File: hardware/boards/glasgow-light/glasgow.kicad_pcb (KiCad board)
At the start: 2 copper layers, 191 parts, among them J1 USB_C_USB2.0, J10 AUX, J2 IDC-Header_2x5_P2.54mm, J3 IDC-Header_2x5_P2.54mm, J4 Conn_01x02, U1 LM358_DFN, U10 SN74LVC1T45DCKR, U11 SN74LVC1T45DCKR, U12 INA180A2, U15 TPD3S014, U16 SN74LVC1T45DCKR, U17 SN74LVC1T45DCKR, U18 SN74LVC1T45DCKR, U19 PCA6408APW, U31 TPS73101DBV, U36 TLV73312PQDRVR, U4 SN74LVC1T45DCKR, U5 ICE40UP5K-SG48ITR, U6 SN74LVC1T45DCKR, U7 GD32VF103, U8 TLV75533PDRVR, U9 SN74LVC1T45DCKR, Y1 8M

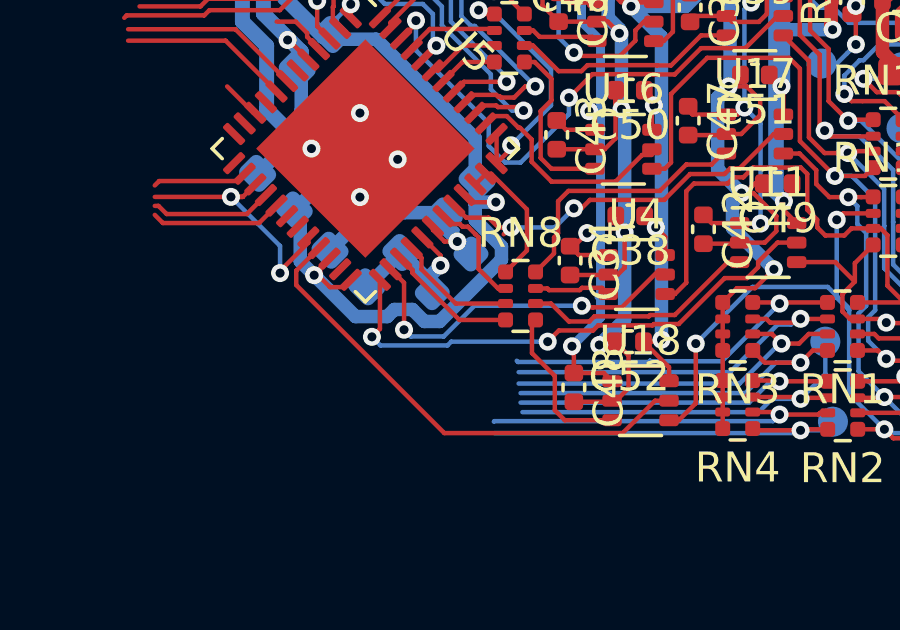
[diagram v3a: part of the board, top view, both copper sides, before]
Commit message: swap some of the DAx pins, again
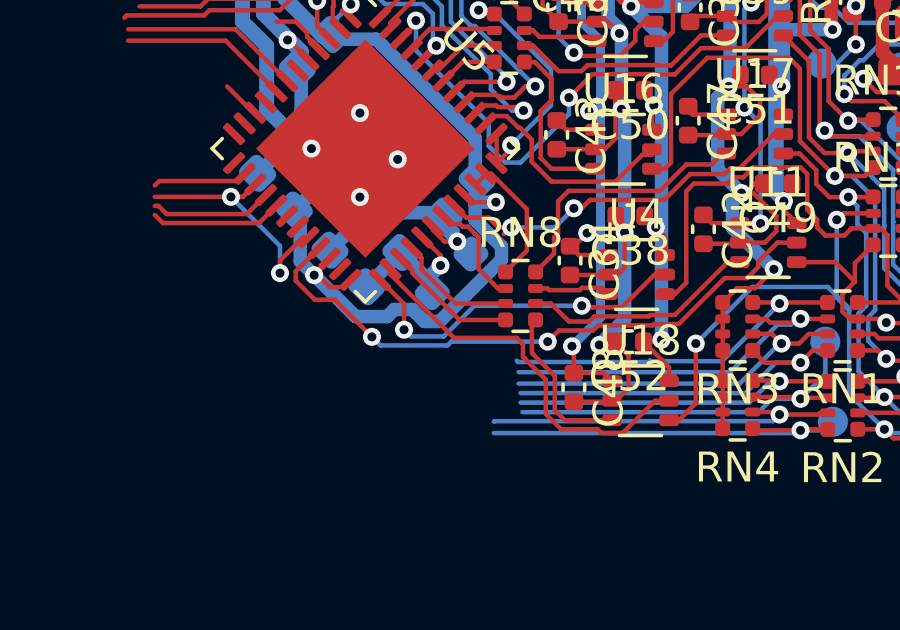
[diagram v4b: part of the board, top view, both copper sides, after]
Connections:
- U5 pad 21: /DA7 -> /DA1
- U5 pad 25: /DA1 -> /DA0
- U5 pad 26: /DA0 -> /DA7
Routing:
- net /DA7: track 16.5 -> 13.0 mm
- net /DA1: track 17.8 -> 20.5 mm
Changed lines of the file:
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@@
     (thickness 1.6)
     (drawings 6)
-    (tracks 1825)
+    (tracks 1836)
     (zones 0)
     (modules 191)
@@
   )
   (setup
-    (last_trace_width 0.45)
+    (last_trace_width 0.15)
     (user_trace_width 0.15)
     (user_trace_width 0.3)
@@
       (net 141 /QA7))
     (pad 26 smd roundrect (at 3.4375 2.25 315) (size 0.875 0.25) (layers F.Cu F.Paste F.Mask) (roundrect_rratio 0.25)
-      (net 140 /DA0))
+      (net 149 /DA7))
     (pad 25 smd roundrect (at 3.4375 2.75 315) (size 0.875 0.25) (layers F.Cu F.Paste F.Mask) (roundrect_rratio 0.25)
-      (net 154 /DA1))
+      (net 140 /DA0))
     (pad 24 smd roundrect (at 2.75 3.4375 315) (size 0.25 0.875) (layers F.Cu F.Paste F.Mask) (roundrect_rratio 0.25)
       (net 2 +3V3))
@@
       (net 2 +3V3))
     (pad 21 smd roundrect (at 1.25 3.4375 315) (size 0.25 0.875) (layers F.Cu F.Paste F.Mask) (roundrect_rratio 0.25)
-      (net 149 /DA7))
+      (net 154 /DA1))
     (pad 20 smd roundrect (at 0.75 3.4375 315) (size 0.25 0.875) (layers F.Cu F.Paste F.Mask) (roundrect_rratio 0.25)
       (net 107 FPGA_SCK))
@@
   (segment (start 135.966884 44.949171) (end 135.723668 45.192387) (width 0.15) (layer F.Cu) (net 106))
   (segment (start 135.903163 45.72) (end 132.969 45.72) (width 0.15) (layer F.Cu) (net 107))
-  (via (at 137.145469 48.26) (size 0.6) (drill 0.3) (layers F.Cu B.Cu) (net 107))
-  (segment (start 137.145469 48.190004) (end 137.145469 48.26) (width 0.15) (layer F.Cu) (net 107))
-  (segment (start 138.088205 47.070492) (end 138.088205 47.247268) (width 0.15) (layer F.Cu) (net 107))
-  (segment (start 138.088205 47.247268) (end 137.145469 48.190004) (width 0.15) (layer F.Cu) (net 107))
   (segment (start 135.903163 45.72) (end 135.509 45.72) (width 0.15) (layer F.Cu) (net 107))
   (segment (start 136.320438 45.302725) (end 135.903163 45.72) (width 0.15) (layer F.Cu) (net 107))
   (via (at 135.509 45.72) (size 0.6) (drill 0.3) (layers F.Cu B.Cu) (net 107))
-  (segment (start 137.145469 47.356469) (end 135.509 45.72) (width 0.15) (layer B.Cu) (net 107))
-  (segment (start 137.145469 48.26) (end 137.145469 47.356469) (width 0.15) (layer B.Cu) (net 107))
+  (via (at 137.14309 48.26) (size 0.6) (drill 0.3) (layers F.Cu B.Cu) (net 107))
+  (segment (start 137.911429 47.070492) (end 137.14309 47.838831) (width 0.15) (layer F.Cu) (net 107))
+  (segment (start 138.088205 47.070492) (end 137.911429 47.070492) (width 0.15) (layer F.Cu) (net 107))
+  (segment (start 137.14309 47.838831) (end 137.14309 48.26) (width 0.15) (layer F.Cu) (net 107))
+  (segment (start 135.509 45.72) (end 137.14309 47.35409) (width 0.15) (layer B.Cu) (net 107))
+  (segment (start 137.14309 47.35409) (end 137.14309 48.26) (width 0.15) (layer B.Cu) (net 107))
   (segment (start 133.365505 46.292187) (end 133.093228 46.01991) (width 0.15) (layer F.Cu) (net 108))
   (segment (start 136.038082 46.292187) (end 133.365505 46.292187) (width 0.15) (layer F.Cu) (net 108))
@@
   (segment (start 141.50306 50.373089) (end 141.278061 50.14809) (width 0.15) (layer B.Cu) (net 140))
   (segment (start 147.202719 49.34869) (end 143.624536 49.34869) (width 0.15) (layer B.Cu) (net 140))
-  (segment (start 140.828243 48.131152) (end 141.278061 48.58097) (width 0.15) (layer F.Cu) (net 140))
   (segment (start 142.600137 50.373089) (end 141.50306 50.373089) (width 0.15) (layer B.Cu) (net 140))
-  (segment (start 141.278061 48.58097) (end 141.278061 50.14809) (width 0.15) (layer F.Cu) (net 140))
   (segment (start 143.624536 49.34869) (end 142.600137 50.373089) (width 0.15) (layer B.Cu) (net 140))
   (via (at 141.278061 50.14809) (size 0.6) (drill 0.3) (layers F.Cu B.Cu) (net 140))
+  (segment (start 141.278061 49.288076) (end 141.278061 50.14809) (width 0.15) (layer F.Cu) (net 140))
+  (segment (start 140.47469 48.484705) (end 141.278061 49.288076) (width 0.15) (layer F.Cu) (net 140))
   (via (at 141.675375 39.842807) (size 0.6) (drill 0.3) (layers F.Cu B.Cu) (net 143))
   (segment (start 141.675375 39.947788) (end 141.675375 39.842807) (width 0.15) (layer F.Cu) (net 143))
@@
   (segment (start 144.23568 40.12168) (end 142.138837 40.12168) (width 0.15) (layer F.Cu) (net 148))
   (segment (start 141.53535 40.725167) (end 141.53535 40.794919) (width 0.15) (layer F.Cu) (net 148))
-  (segment (start 142.621 53.594) (end 137.684902 48.657902) (width 0.15) (layer F.Cu) (net 149))
-  (segment (start 150.1115 52.5145) (end 149.645994 52.5145) (width 0.15) (layer F.Cu) (net 149))
-  (segment (start 137.684902 48.657902) (end 137.684902 48.180901) (width 0.15) (layer F.Cu) (net 149))
-  (segment (start 149.645994 52.5145) (end 148.566494 53.594) (width 0.15) (layer F.Cu) (net 149))
-  (segment (start 148.566494 53.594) (end 142.621 53.594) (width 0.15) (layer F.Cu) (net 149))
-  (segment (start 137.684902 48.180901) (end 138.441758 47.424045) (width 0.15) (layer F.Cu) (net 149))
+  (segment (start 148.571084 53.58941) (end 149.645994 52.5145) (width 0.15) (layer F.Cu) (net 149))
+  (segment (start 147.726916 53.46441) (end 147.851916 53.58941) (width 0.15) (layer F.Cu) (net 149))
+  (segment (start 146.00409 51.813226) (end 146.004091 52.956227) (width 0.15) (layer F.Cu) (net 149))
+  (segment (start 146.512274 53.46441) (end 147.726916 53.46441) (width 0.15) (layer F.Cu) (net 149))
+  (segment (start 145.242091 51.051227) (end 146.00409 51.813226) (width 0.15) (layer F.Cu) (net 149))
+  (segment (start 145.24209 50.62709) (end 145.242091 51.051227) (width 0.15) (layer F.Cu) (net 149))
+  (segment (start 145.034 50.419) (end 145.24209 50.62709) (width 0.15) (layer F.Cu) (net 149))
+  (segment (start 146.004091 52.956227) (end 146.512274 53.46441) (width 0.15) (layer F.Cu) (net 149))
+  (segment (start 142.939315 50.419) (end 145.034 50.419) (width 0.15) (layer F.Cu) (net 149))
+  (segment (start 147.851916 53.58941) (end 148.571084 53.58941) (width 0.15) (layer F.Cu) (net 149))
+  (segment (start 140.828243 48.307928) (end 142.939315 50.419) (width 0.15) (layer F.Cu) (net 149))
+  (segment (start 149.645994 52.5145) (end 150.1115 52.5145) (width 0.15) (layer F.Cu) (net 149))
+  (segment (start 140.828243 48.131152) (end 140.828243 48.307928) (width 0.15) (layer F.Cu) (net 149))
   (via (at 145.371176 38.856147) (size 0.6) (drill 0.3) (layers F.Cu B.Cu) (net 150))
   (segment (start 149.977 36.957) (end 149.75209 37.18191) (width 0.15) (layer F.Cu) (net 150))
@@
   (segment (start 144.573323 38.108406) (end 144.343474 38.108406) (width 0.15) (layer B.Cu) (net 153))
   (via (at 140.208 50.385156) (size 0.6) (drill 0.3) (layers F.Cu B.Cu) (net 154))
-  (segment (start 140.47469 50.118466) (end 140.208 50.385156) (width 0.15) (layer F.Cu) (net 154))
-  (segment (start 140.47469 48.484705) (end 140.47469 50.118466) (width 0.15) (layer F.Cu) (net 154))
   (segment (start 140.495844 50.673) (end 140.208 50.385156) (width 0.15) (layer B.Cu) (net 154))
   (segment (start 142.724364 50.673) (end 140.495844 50.673) (width 0.15) (layer B.Cu) (net 154))
   (segment (start 142.851673 50.545691) (end 142.724364 50.673) (width 0.15) (layer B.Cu) (net 154))
   (segment (start 146.06691 50.545691) (end 142.851673 50.545691) (width 0.15) (layer B.Cu) (net 154))
+  (segment (start 138.113803 47.752) (end 138.441758 47.424045) (width 0.15) (layer F.Cu) (net 154))
+  (segment (start 137.668 48.197803) (end 138.113803 47.752) (width 0.15) (layer F.Cu) (net 154))
+  (segment (start 137.668 48.514) (end 137.668 48.197803) (width 0.15) (layer F.Cu) (net 154))
+  (segment (start 138.303 49.149) (end 137.668 48.514) (width 0.15) (layer F.Cu) (net 154))
+  (segment (start 138.971844 49.149) (end 138.303 49.149) (width 0.15) (layer F.Cu) (net 154))
+  (segment (start 140.208 50.385156) (end 138.971844 49.149) (width 0.15) (layer F.Cu) (net 154))
   (segment (start 136.320438 42.916239) (end 136.261239 42.916239) (width 0.15) (layer F.Cu) (net 155))
   (segment (start 136.261239 42.916239) (end 135.382 42.037) (width 0.15) (layer F.Cu) (net 155))

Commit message: something
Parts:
- R9: value 15k -> 10k
- moved C12 10.6 mm to (109.6, 47.1), turned to 180 degrees
- moved C11 5.04 mm to (106.8, 50.2), turned to 90 degrees
- moved R35 1.62 mm to (162.4, 37.6)
- moved R33 1.49 mm to (161.3, 36.4)
- moved C3 0.47 mm to (101.2, 49.6), turned to 135 degrees
- moved C2 0.45 mm to (97.5, 41.5), turned to 45 degrees
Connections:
- net /FPGA_JTAG3 renamed Net-(U7-Pad43)
- net /FPGA_JTAG4 renamed Net-(U7-Pad45)
- U7 pad 29: /LED_ACT -> /CLKREF
- U7 pad 31: /CLKREF -> /LED_ACT
- U7 pad 41: /FPGA_JTAG1 -> /~FPGA_RESET
- U7 pad 42: /FPGA_JTAG2 -> /FPGA_DONE
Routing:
- net ADC5: track 14.2 -> 23.2 mm
- net ADC4: track 11.4 -> 20.3 mm
- net ADC3: track 12.6 -> 21.5 mm
- net ADC1: track 12.7 -> 21.6 mm
- net ADC2: track 12.1 -> 20.9 mm
- net ADC0: track 12.2 -> 20.9 mm
- net /IO_Banks/VIOA: track 143.0 -> 134.6 mm
- net ADC6: track 12.2 -> 20.2 mm
- net ADC7: track 14.0 -> 22.0 mm
- net /LED_ACT: track 0.00 -> 7.67 mm, vias 0 -> 1
- net FPGA_MOSI: track 4.41 -> 11.3 mm, vias 0 -> 1
- net FPGA_MISO: track 3.16 -> 9.42 mm, vias 0 -> 1
- net FPGA_SCK: track 8.82 -> 14.7 mm, vias 2 -> 3
- net FPGA_CS: track 4.08 -> 9.42 mm, vias 0 -> 1
- net VIO_DAC: track 62.0 -> 61.0 mm, vias 2 -> 1
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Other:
- board outline added: 90.2 x 21 mm

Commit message: add GD32VF103T in QFN36 package
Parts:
- added U2: GD32VF103T, Package_DFN_QFN:QFN-36-1EP_6x6mm_P0.5mm_EP4.1x4.1mm, F.Cu at (122.7, 44.7)
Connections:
- net Net-(C17-Pad1) renamed /NRST
- net Net-(R10-Pad1) renamed /VDDA
- net Net-(R17-Pad2) renamed /BOOT0

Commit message: .
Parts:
- added RN13: 33R, Glasgow:R_Array_Convex_4x0402, F.Cu at (134.9, 48.8)
- added TP6: SYNC, TestPoint:TestPoint_Pad_D1.0mm, F.Cu at (144.9, 52.3)
- TP40: renamed from TP6; value USBGND -> TMS
- TP41: renamed from TP7; value USBGND -> TCK
- TP42: renamed from TP18; value USBGND -> TDI
- TP43: renamed from TP20; value USBGND -> TDO
- moved TP42 82.5 mm to (137.3, 52.3)
- moved TP40 80.5 mm to (142.4, 52.3)
- moved TP41 79.4 mm to (139.8, 52.3)
- moved TP43 68.3 mm to (134.7, 52.3)
- moved C4 28.6 mm to (133.8, 43.0)
- moved C11 28.1 mm to (128.1, 31.9)
- moved Y1 28.1 mm to (130.8, 31.1)
- moved C12 28.1 mm to (130.9, 28.8)
- moved C3 26.3 mm to (127.5, 48.6)
- moved C2 26.0 mm to (123.3, 44.1), turned to 90 degrees
- moved TP21 22.9 mm to (71.9, 37.5)
- moved U2 6.28 mm to (128.9, 44.1), turned to 225 degrees
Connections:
- TP40 pad 1: Net-(TP6-Pad1) -> /TMS
- TP41 pad 1: Net-(TP7-Pad1) -> /TCK
- TP42 pad 1: Net-(TP18-Pad1) -> /TDI
- TP43 pad 1: Net-(TP20-Pad1) -> /TDO
- U2 pad 25: Net-(U2-Pad25) -> /FPGA_DONE
- U2 pad 28: (no net) -> /~FPGA_RESET
- U2 pad 29: (no net) -> FPGA_CS
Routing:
- net +3V3: track 205.9 -> 237.5 mm, vias 17 -> 20
- net GND: track 283.3 -> 310.3 mm, vias 27 -> 29
- net VIO_CURRENT: track 74.0 -> 50.4 mm, vias 2 -> 1
- net VIO_DAC: track 61.0 -> 42.4 mm
- net /~SYNC: track 1.30 -> 17.7 mm, vias 0 -> 2
- net ADC7: track 22.0 -> 38.3 mm
- net ADC6: track 20.2 -> 35.9 mm
- net ADC5: track 23.2 -> 38.3 mm
- net ADC4: track 20.3 -> 35.0 mm
- net ADC3: track 21.5 -> 35.8 mm
- net ADC2: track 20.9 -> 34.8 mm
- net ADC1: track 21.6 -> 35.0 mm
- net ADC0: track 20.9 -> 34.1 mm
- net /FPGA_DONE: track 6.02 -> 19.1 mm, vias 0 -> 2
- net /TMS: track 0.00 -> 8.13 mm
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
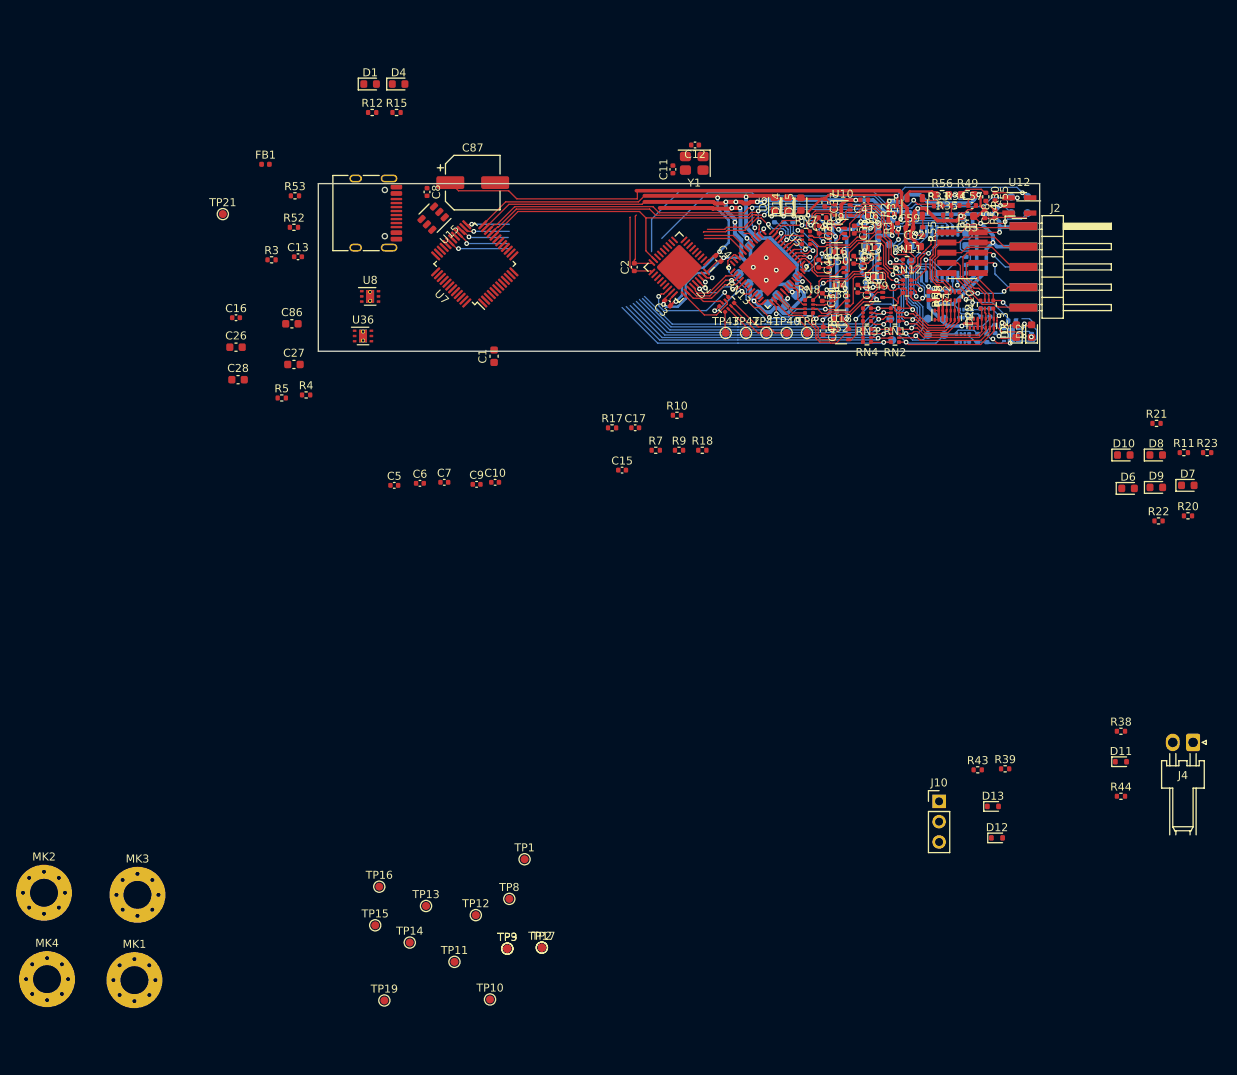
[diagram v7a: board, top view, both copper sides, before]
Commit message: rotate GD32 -> routing is *much* easier
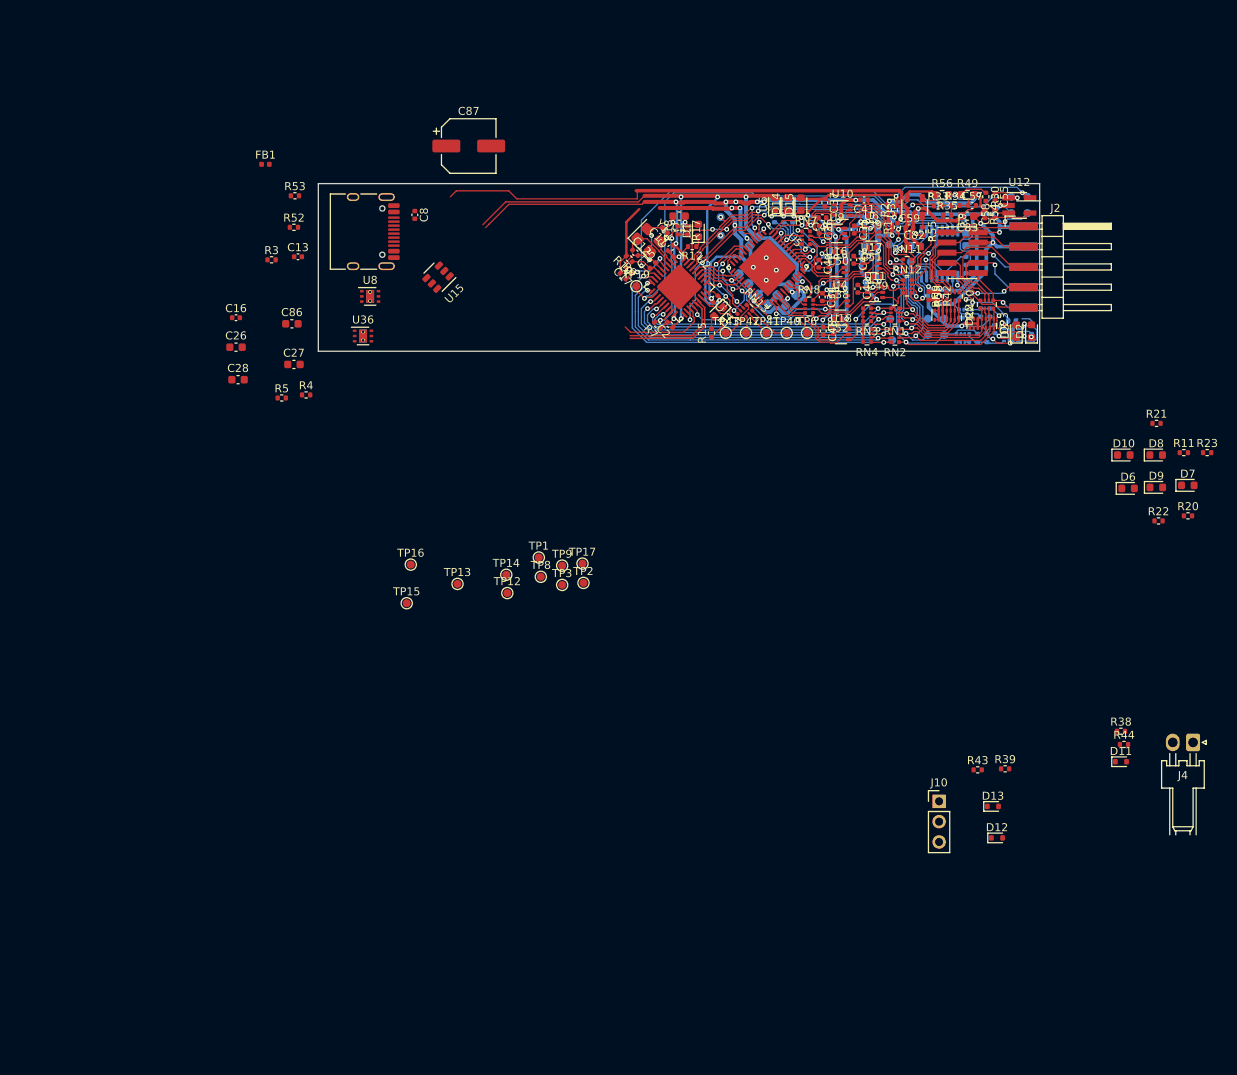
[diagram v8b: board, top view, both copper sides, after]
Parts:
- removed C10, C5, C6, C7, C9: u1, Capacitor_SMD:C_0402_1005Metric
- removed MK1, MK2, MK3, MK4: Mounting_Hole_PAD, Glasgow:MountingHole_3.5mm_Pad_Via_CrtYd
- removed TP21: USBGND, TestPoint:TestPoint_Pad_D1.0mm
- removed U7: GD32VF103, Package_QFP:LQFP-48_7x7mm_P0.5mm
- TP10, TP11: moved to B.Cu
- moved TP10 102.0 mm to (134.1, 37.8)
- moved TP11 96.7 mm to (134.1, 40.1)
- moved TP19 94.7 mm to (123.6, 46.5)
- moved D4 49.1 mm to (133.9, 49.7), turned to 225 degrees
- moved TP9 48.4 mm to (114.3, 81.4)
- moved TP17 48.3 mm to (116.8, 81.2)
- moved R15 48.1 mm to (133.0, 52.3), turned to 90 degrees
- moved TP14 47.5 mm to (107.3, 82.5)
- moved TP3 46.0 mm to (114.3, 83.8)
- moved TP2 45.9 mm to (117.0, 83.6)
- moved D1 44.9 mm to (131.3, 39.5), turned to 90 degrees
- moved R12 43.4 mm to (130.6, 41.5), turned to 180 degrees
- moved TP12 40.5 mm to (107.4, 84.8)
- moved TP13 40.5 mm to (101.2, 83.7)
- moved TP15 40.5 mm to (94.9, 86.1)
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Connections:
- C15 pad 1: GND -> /VDDA
- C15 pad 2: Net-(C15-Pad2) -> GND
- D1 pad 1: GND -> Net-(D1-Pad1)
- D1 pad 2: Net-(D1-Pad2) -> +3V3
- R12 pad 1: +3V3 -> Net-(D1-Pad1)
- R12 pad 2: Net-(D1-Pad2) -> GND
- U2 pad 10: ADC3 -> ADC5
- U2 pad 12: ADC7 -> ADC4
- U2 pad 13: ADC4 -> ADC3
- U2 pad 14: ADC5 -> ADC2
- U2 pad 15: ADC6 -> ADC1
- U2 pad 16: VIO_CURRENT -> ADC0
- U2 pad 7: ADC0 -> VIO_CURRENT
- U2 pad 8: ADC1 -> ADC7
- U2 pad 9: ADC2 -> ADC6
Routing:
- net GND: track 310.3 -> 337.5 mm, vias 29 -> 34
- net /SCL: track 68.3 -> 44.1 mm
- net /SDA: track 67.7 -> 44.5 mm
- net +3V3: track 237.5 -> 256.5 mm, vias 20 -> 23
- net VIO_ENA: track 63.0 -> 48.7 mm, vias 2 -> 6
- net /USB_P: track 0.00 -> 13.5 mm
- net /USB_N: track 0.00 -> 12.7 mm
- net +5V: track 65.8 -> 77.0 mm
- net /CLKREF: track 13.5 -> 24.2 mm, vias 2 -> 4
- net VIO_CURRENT: track 50.4 -> 60.8 mm, vias 1 -> 2
- net VIO_DAC: track 42.4 -> 52.3 mm, vias 1 -> 2
- net FPGA_SCK: track 22.5 -> 13.0 mm, vias 4 -> 3
- net FPGA_MISO: track 13.1 -> 5.27 mm, vias 1 -> 0
- net /XTALIN: track 0.00 -> 7.30 mm
- net /NRST: track 0.00 -> 6.99 mm, vias 0 -> 2
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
